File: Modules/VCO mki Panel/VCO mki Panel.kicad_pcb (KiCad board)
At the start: 2 copper layers, 100 x 200 mm, 34 parts

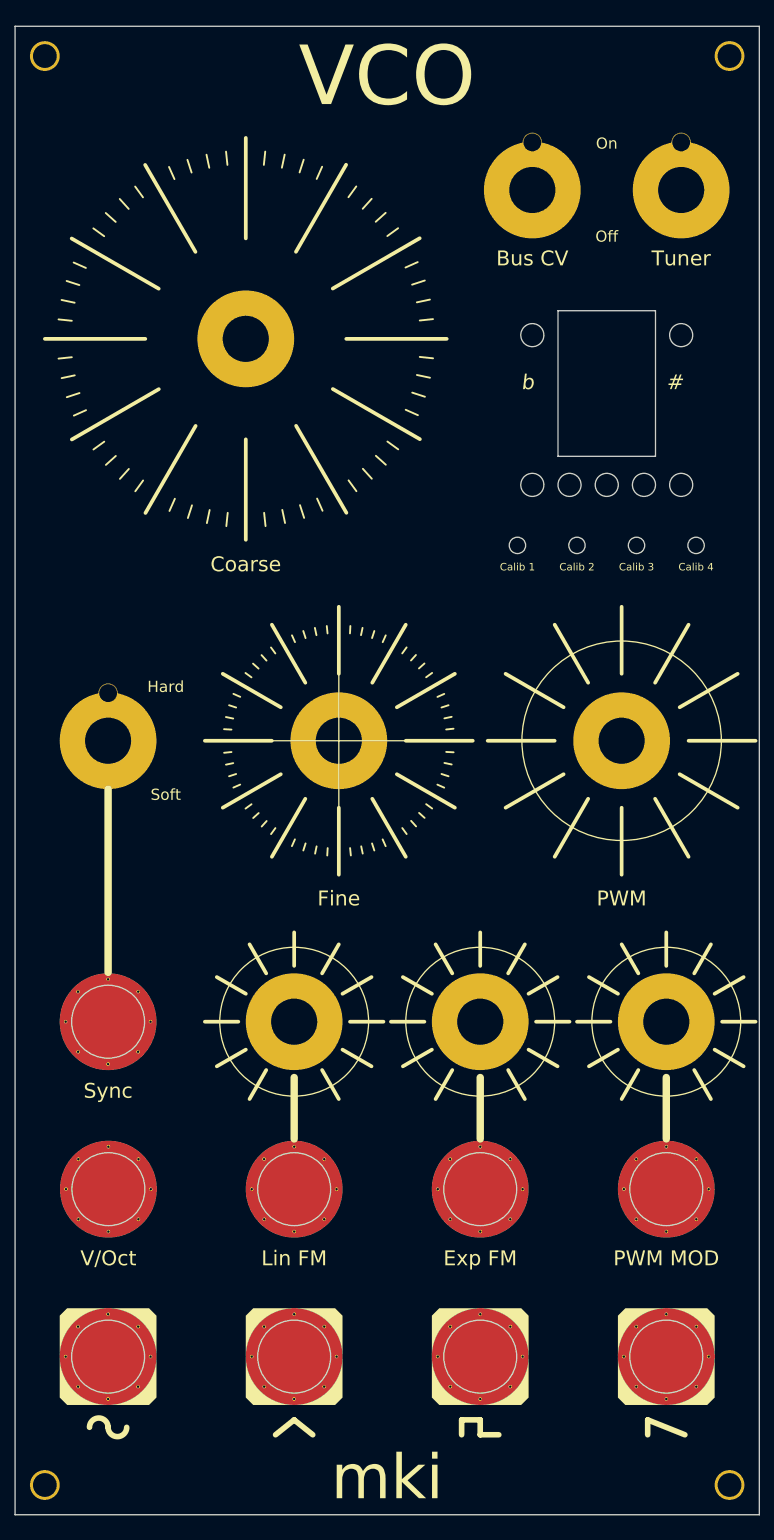
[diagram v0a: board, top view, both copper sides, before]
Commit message: Synced SCH to PCB
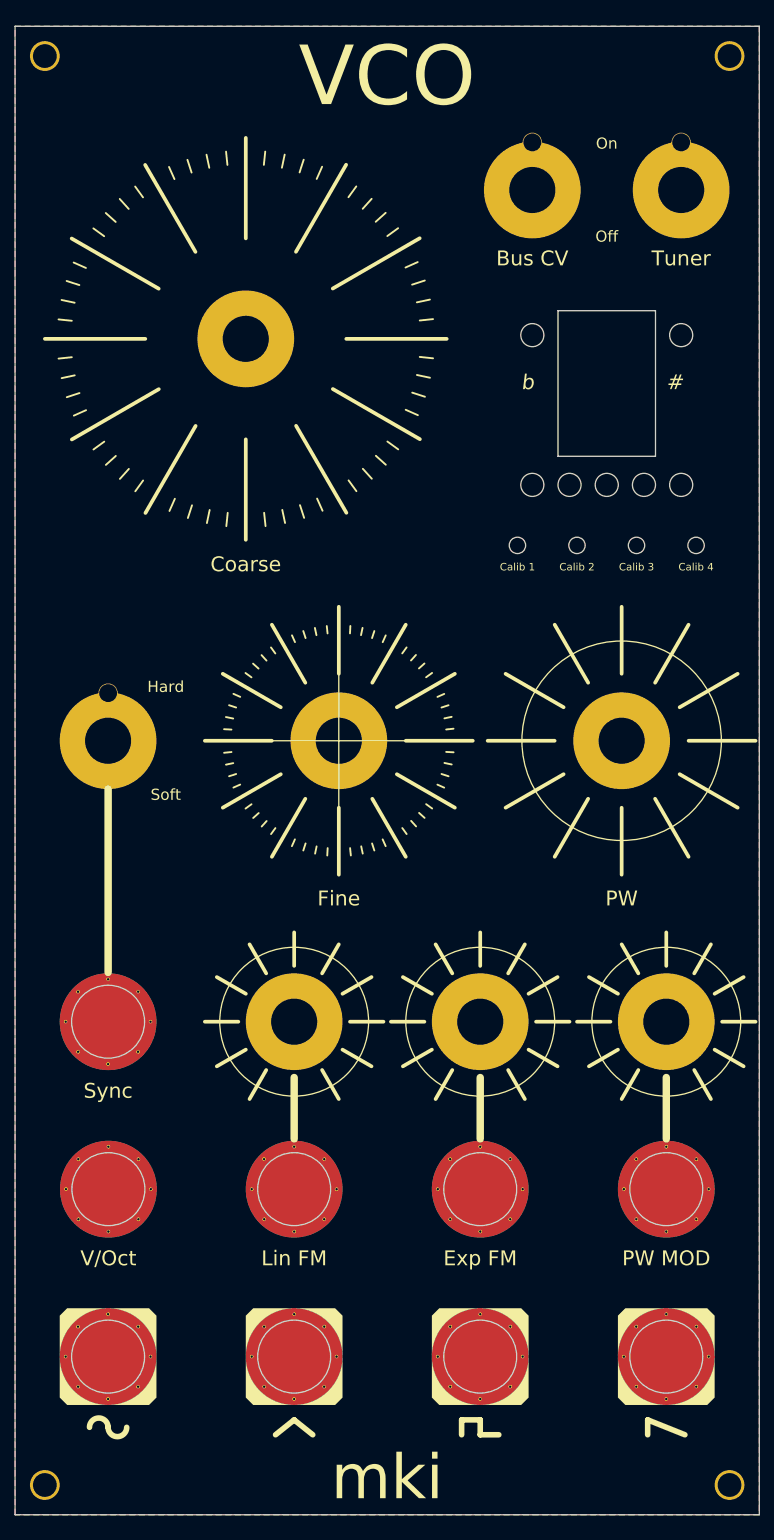
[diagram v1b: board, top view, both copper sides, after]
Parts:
- H10: value FM Lin -> Lin FM
- H11: value PWM Mod -> Exp FM
- H12: value Shape Mod -> PW Mod
- H20: value PWM MOD -> PW MOD
- H28: renamed from REF**; value Hard Sync -> Soft Hard
- H29: renamed from REF**; value MountingHole_LED_3mm -> LED_b
- H30: renamed from REF**; value MountingHole_LED_3mm -> LED_#
- H31: renamed from REF**; value MountingHole_LED_3mm -> LED_-2
- H32: renamed from REF**; value MountingHole_LED_3mm -> LED_-1
- H33: renamed from REF**; value MountingHole_LED_3mm -> LED_0
- H34: renamed from REF**; value MountingHole_LED_3mm -> LED_+1
- H35: renamed from REF**; value MountingHole_LED_3mm -> LED_+2
- H6: renamed from REF**; value 7Segment_Cutout -> 7Segment
- H8: value PWM -> PW
- renumbered H24 to H25, REF** to H26, REF** to H27
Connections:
- H26 pad 1: (no net) -> GND
- H27 pad 1: (no net) -> GND
- H28 pad 1: (no net) -> GND
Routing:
- added copper zone on B.Cu, net GND
- added copper zone on F.Cu, net GND

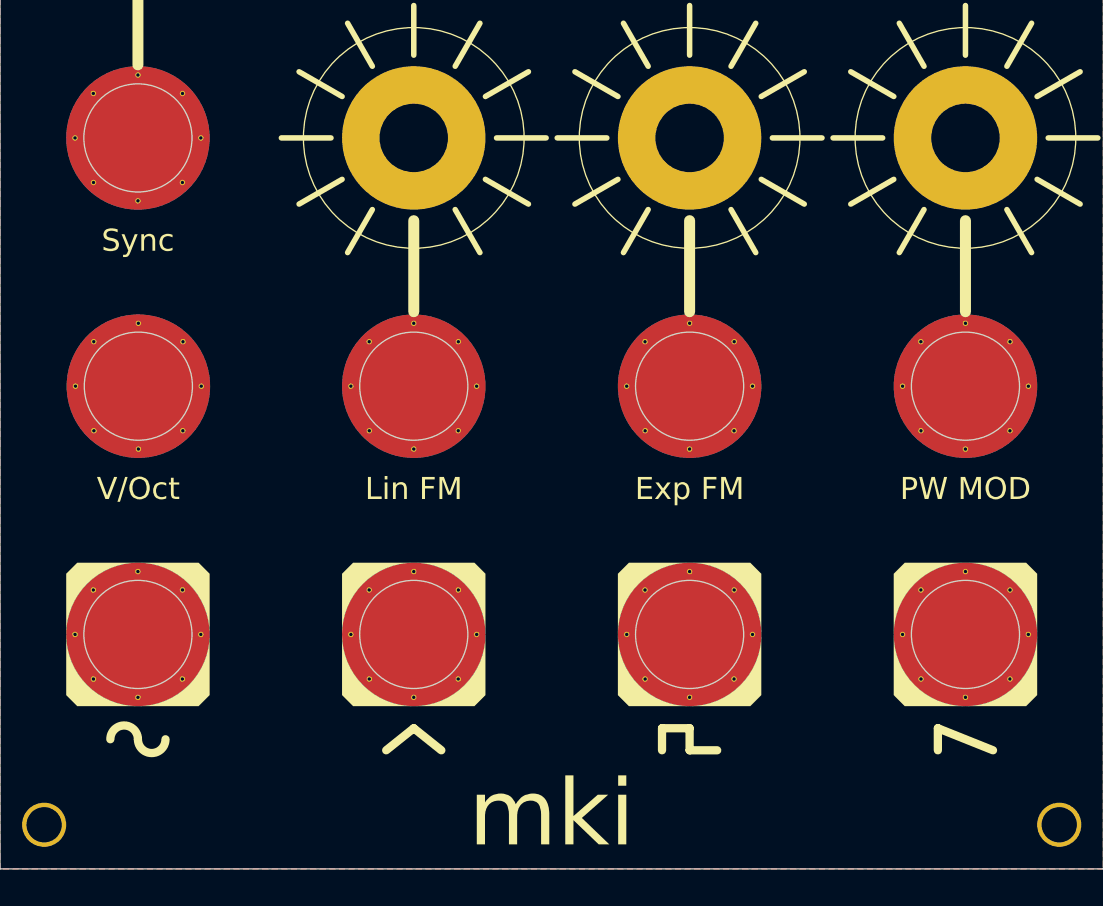
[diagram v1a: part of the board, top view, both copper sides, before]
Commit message: Updated jack footprints to 12mm washer
... and added hash art to Adapter Mult CV and Gate jacks
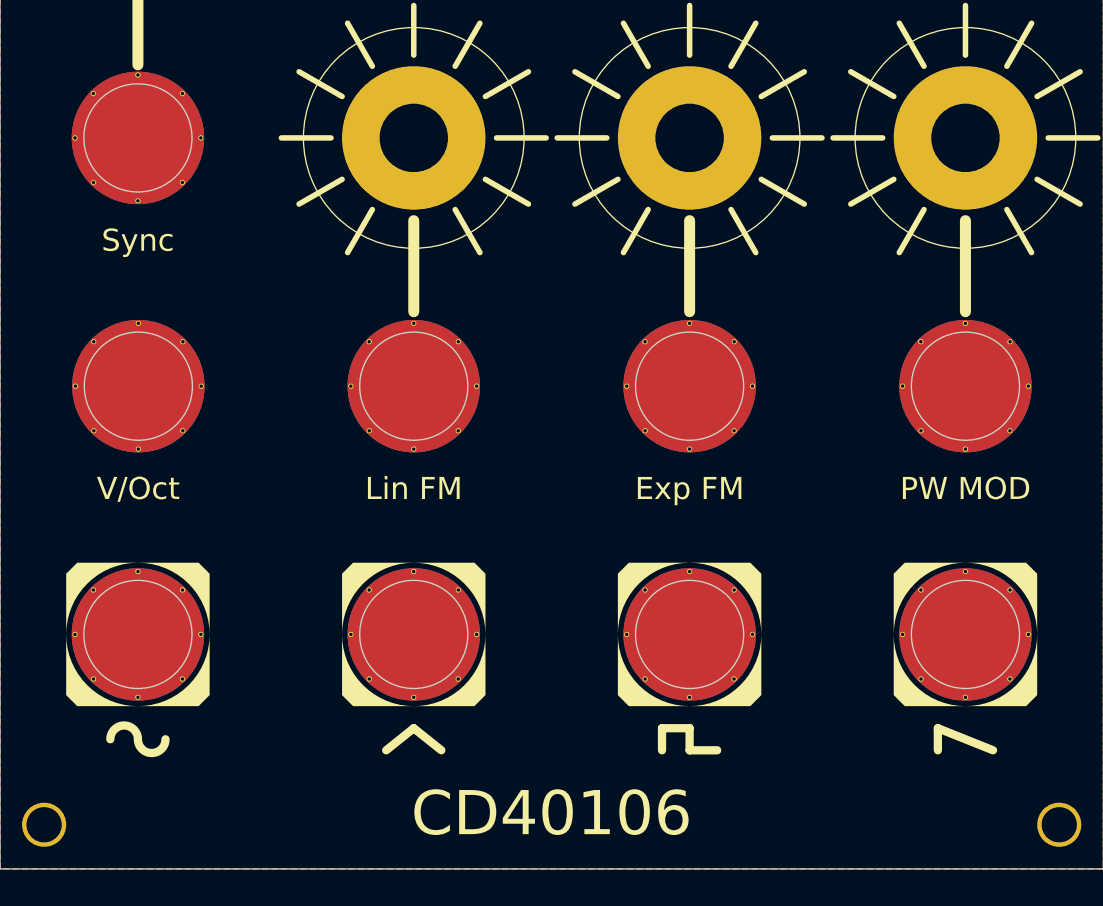
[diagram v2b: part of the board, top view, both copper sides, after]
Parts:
- H1, H2, H3, H4: footprint SynthStuff:MountingHole_3.2mm_M3_Pad4mm -> SynthStuff:MountingHole_Rails
- H13, H14, H15, H16: footprint SynthStuff:Jack_6.35mm_Cutout_Output_v5 -> SynthStuff:Jack_6.35mm_Cutout_Output_v6
- H17, H18, H19, H20, H25: footprint SynthStuff:Jack_6.35mm_Cutout_v2 -> SynthStuff:Jack_6.35mm_Cutout_v3
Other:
- board text added: "CD40106"
- board text removed: "mki"

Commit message: More adjustments to panel
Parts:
- added J1: GND, Connector_Wire:SolderWirePad_1x01_SMD_5x10mm, B.Cu at (56.8, 125.0)
- H8: value PW -> Pulse Width
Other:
- board text added: "JLCJLCJLCJLC"
- board text added: "Mk1 - June 2024"

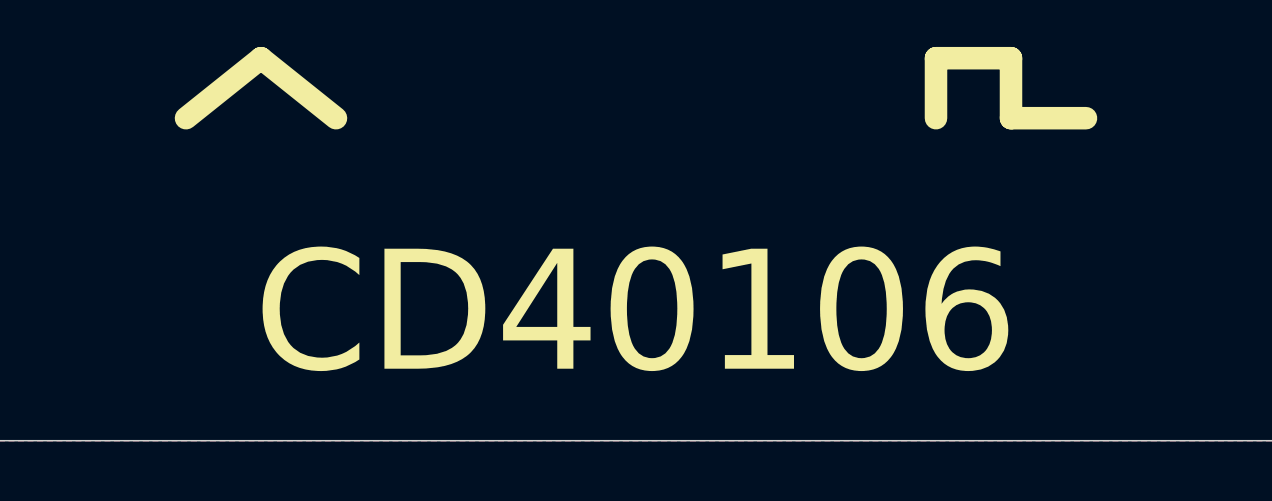
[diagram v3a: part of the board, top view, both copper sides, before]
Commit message: Changed font of VCO type decal
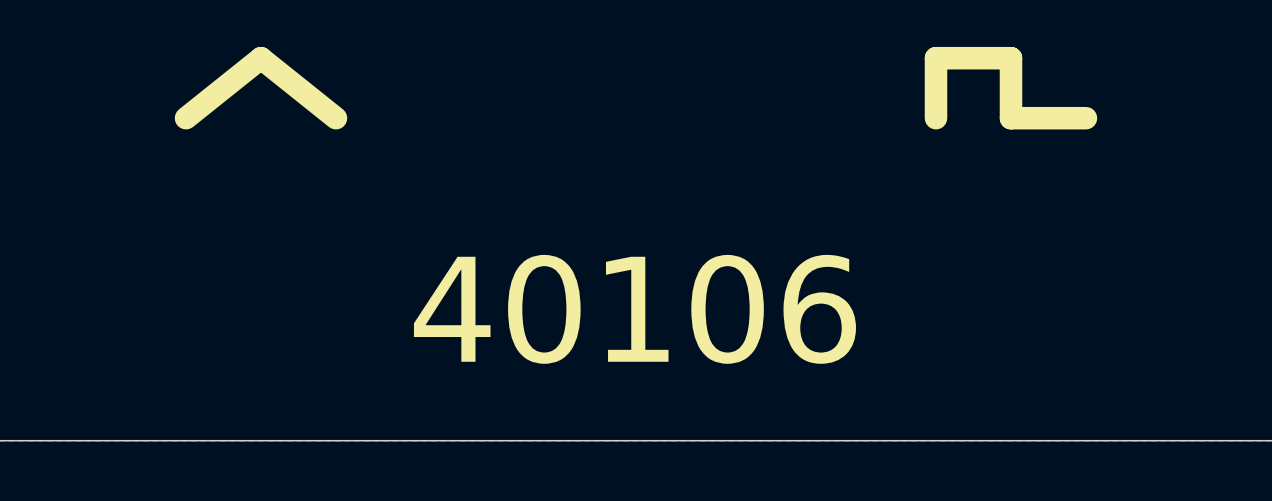
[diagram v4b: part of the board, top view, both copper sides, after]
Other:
- board text added: "40106"
- board text removed: "CD40106"

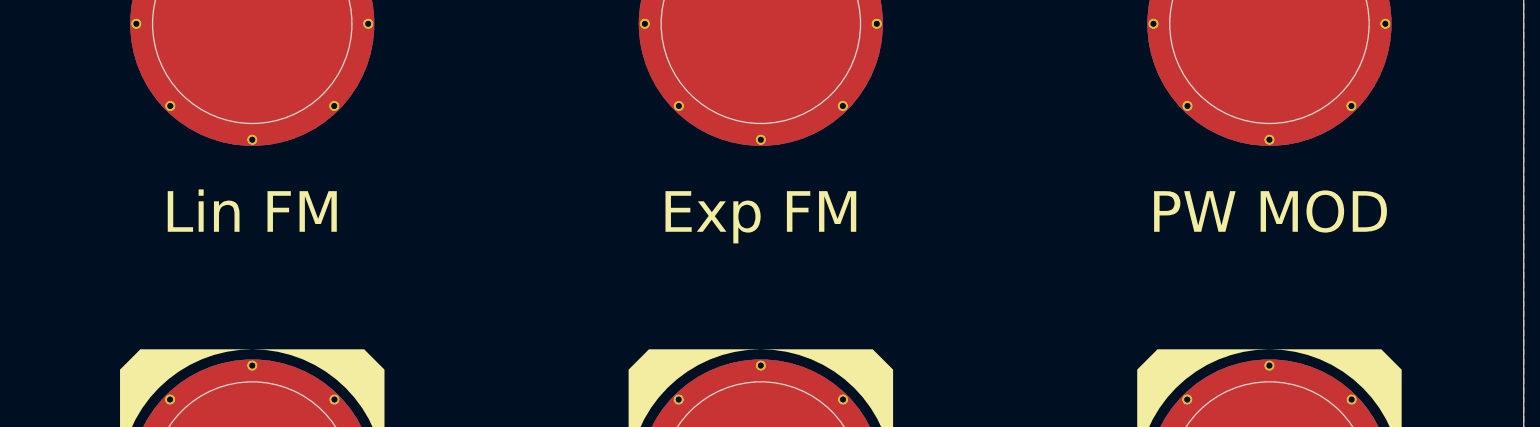
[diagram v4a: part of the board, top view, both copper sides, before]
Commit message: Created VCO sub sheets
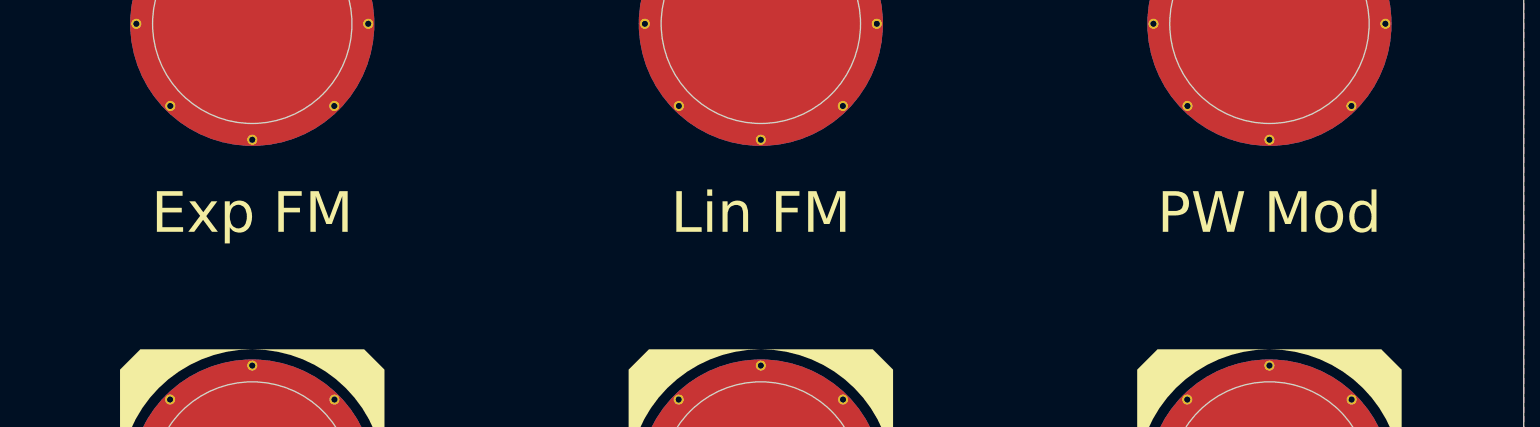
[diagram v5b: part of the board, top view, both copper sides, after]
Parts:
- H10, H18: value Lin FM -> Exp FM
- H11, H19: value Exp FM -> Lin FM
- H20: value PW MOD -> PW Mod
